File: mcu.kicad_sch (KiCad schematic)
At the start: 13 parts, among them J1 Micro_SD_Card, J2 Conn_01x40, J3 USB_C_Receptacle_USB2.0_14P, U1 ESP32-S3-WROOM-1

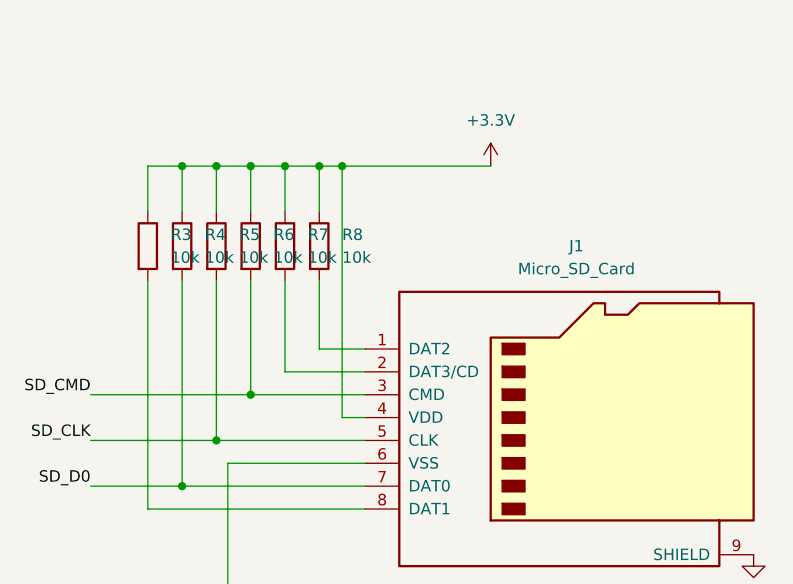
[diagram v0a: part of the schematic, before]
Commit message: add sensors sheet
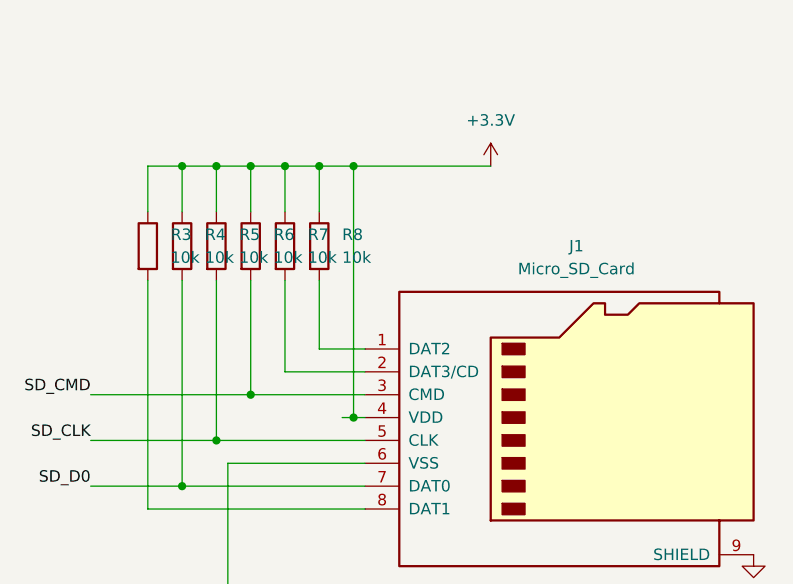
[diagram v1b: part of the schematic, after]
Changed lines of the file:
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@@
+	)
+	(junction
+		(at 195.58 95.25)
+		(diameter 0)
+		(color 0 0 0 0)
 	)
 	(junction
@@
 	)
 	(junction
-		(at 194.31 95.25)
+		(at 195.58 123.19)
 		(diameter 0)
 		(color 0 0 0 0)
@@
 	(wire
 		(pts
+			(xy 195.58 95.25) (xy 210.82 95.25)
+		)
+		(stroke
+			(width 0)
+			(type default)
+		)
+	)
+	(wire
+		(pts
 			(xy 176.53 95.25) (xy 176.53 100.33)
 		)
@@
 	(wire
 		(pts
-			(xy 194.31 95.25) (xy 210.82 95.25)
-		)
-		(stroke
-			(width 0)
-			(type default)
-		)
-	)
-	(wire
-		(pts
 			(xy 181.61 128.27) (xy 181.61 143.51)
 		)
@@
 	(wire
 		(pts
+			(xy 195.58 123.19) (xy 194.31 123.19)
+		)
+		(stroke
+			(width 0)
+			(type default)
+		)
+	)
+	(wire
+		(pts
 			(xy 176.53 130.81) (xy 196.85 130.81)
 		)
@@
 	(wire
 		(pts
-			(xy 196.85 123.19) (xy 194.31 123.19)
+			(xy 196.85 123.19) (xy 195.58 123.19)
 		)
 		(stroke
@@
 	(wire
 		(pts
-			(xy 191.77 95.25) (xy 194.31 95.25)
-		)
-		(stroke
-			(width 0)
-			(type default)
-		)
-	)
-	(wire
-		(pts
-			(xy 194.31 123.19) (xy 194.31 95.25)
-		)
-		(stroke
+			(xy 191.77 95.25) (xy 195.58 95.25)
+		)
+		(stroke
+			(width 0)
+			(type default)
+		)
+	)
+	(wire
+		(pts
+			(xy 195.58 123.19) (xy 195.58 95.25)
+		)
+		(stroke
